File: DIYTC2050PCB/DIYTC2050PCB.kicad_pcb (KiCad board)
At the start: 2 copper layers, 17.5 x 13 mm, 8 parts, among them J1 TC2050-IDC

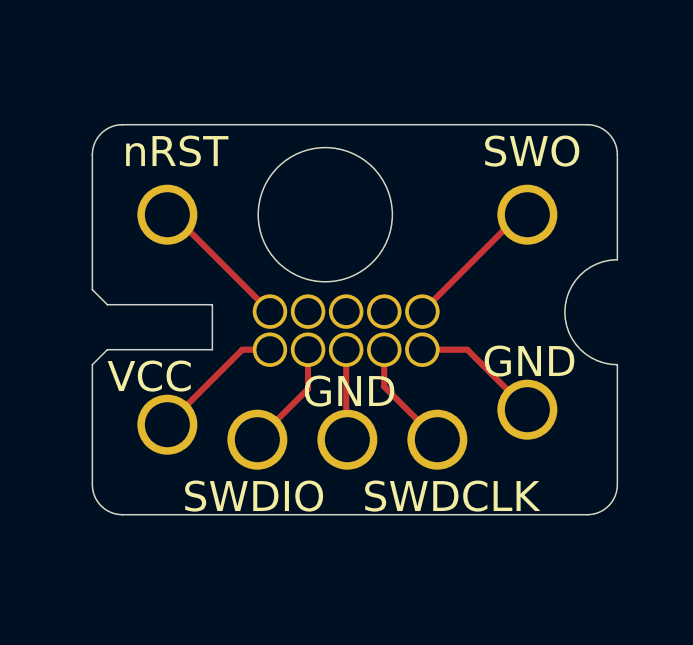
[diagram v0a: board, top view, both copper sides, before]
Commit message: Enlarge PCB and soldering holes
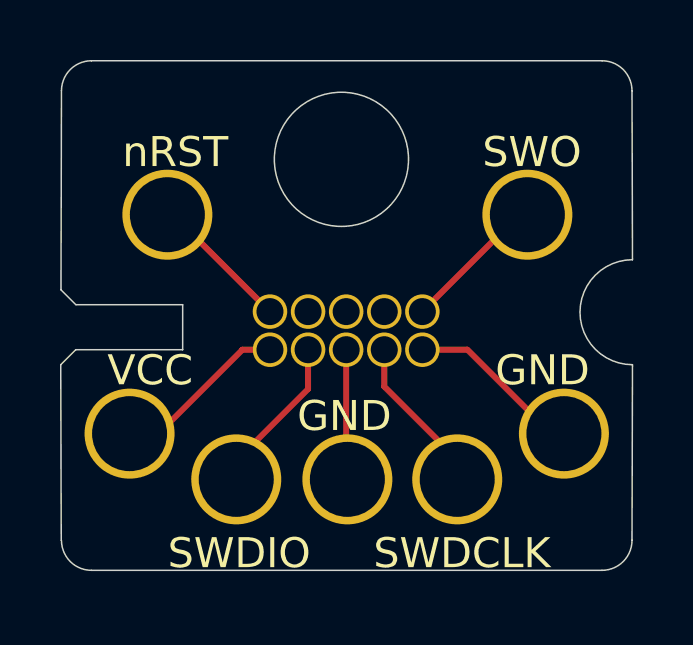
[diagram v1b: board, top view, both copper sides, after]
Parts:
- J11, J2, J3, J4, J5, J6, J7: footprint THTCabble:THTCable_1.5mm -> THTCabble:THTCable_2.5mm
- moved J3 1.50 mm to (145.8, 99.8)
- moved J5 1.48 mm to (153.2, 99.8)
- moved J6 1.46 mm to (156.7, 98.3)
- moved J4 1.32 mm to (149.5, 99.8)
- moved J2 1.29 mm to (142.2, 98.3)
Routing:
- net Net-(J1-SWDIO): track 3.70 -> 5.57 mm
- net Net-(J1-SWDCLK): track 3.73 -> 5.33 mm
- net Net-(J1-GND-Pad3): track 3.02 -> 4.59 mm
- net Net-(J1-GND-Pad5): track 4.33 -> 5.88 mm
- net Net-(J1-VCC): track 4.46 -> 5.58 mm
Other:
- board size 17.5 x 13 mm -> 19.1 x 17 mm

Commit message: Add PCB Rev1.1
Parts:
- removed J11, J3, J4, J5, J6, J7: ~, THTCabble:THTCable_2.5mm
- J2: value ~ -> Conn_01x06_Pin; footprint THTCabble:THTCable_2.5mm -> Connector_PinHeader_2.54mm:PinHeader_1x06_P2.54mm_Vertical
- moved J2 2.86 mm to (143.2, 101.0), turned to 90 degrees
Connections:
- net Net-(J1-VCC) renamed +3V3
- J1 pad 10: Net-(J1-nRST) -> nRST
- J1 pad 2: Net-(J1-SWDIO) -> SWDIO
- J1 pad 3: Net-(J1-GND-Pad3) -> GND
- J1 pad 4: Net-(J1-SWDCLK) -> SWDCLK
- J1 pad 5: Net-(J1-GND-Pad5) -> GND
- J1 pad 6: Net-(J1-SWO) -> SWO
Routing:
- net SWO: track 0.00 -> 15.5 mm
- net GND: track 0.00 -> 10.7 mm
- net nRST: track 0.00 -> 8.38 mm
- net SWDCLK: track 0.00 -> 6.58 mm
- net SWDIO: track 0.00 -> 6.58 mm
- net Net-(J1-GND-Pad5): track 5.88 -> 0.00 mm
- net Net-(J1-SWDIO): track 5.57 -> 0.00 mm
- net Net-(J1-SWDCLK): track 5.33 -> 0.00 mm
- net Net-(J1-SWO): track 4.84 -> 0.00 mm
- net Net-(J1-nRST): track 4.76 -> 0.00 mm
- net Net-(J1-GND-Pad3): track 4.59 -> 0.00 mm
- net +3V3: track 5.58 -> 7.05 mm
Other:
- board text added: "P90s DIY TC2050"
- board text added: "Rev1.1"
- board text added: "SW CLK"
- board text added: "SW DIO"
- board text removed: "SWDCLK"
- board text removed: "SWDIO"
